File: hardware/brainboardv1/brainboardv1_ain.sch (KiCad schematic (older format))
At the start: 27 parts

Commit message: Nearly finished v1 sch & brd, await final check
Fixed errors from Rev 0, added MPU-6050 accelerometer/gyro for head
motion tracking, switched to +/-2.5V analog supply, added 2 bipolar
analog inputs for EOG tracking, added daisy-chain capability
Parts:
- removed P?: CONN_12, ~, symbol CONN_12
- added C55, C56: 4.7nF, ~, symbol C
- added P2: CONN_14, ~, symbol CONN_14
- added R21, R23: 4.99K, ~, symbol R
- gave numbers to parts that had none: 26
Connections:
- net labels added: +2.5V, -2.5V, CH1ELEC_N, CH2ELEC_N
- net labels removed: +5VA, AIN3N, AIN4N, AIN5N, AIN6N, AIN7N, AIN8N
- wire segments 67 -> 78
- no-connect marks 10 -> 1
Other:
- note added: "Channels 3-8 are single-ended only. Channels 1 and 2 can be configured as bipolar\nfor auxilliary signals like EOG, EMG, ECG, etc."
- note removed: "Rev. 0 is single-ended only. This saves board space\nand appears to be the dominant EEG BCI mode in any\ncase."
- moved on the sheet: C20, C21, C22, C23, C24, C25, C26, C27, C28, R11, R12, R13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

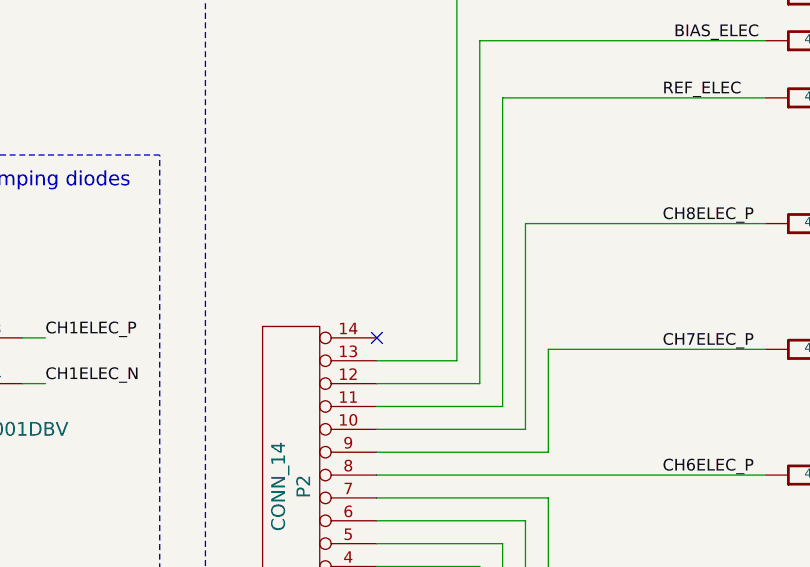
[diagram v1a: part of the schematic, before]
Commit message: Added thicker power traces and fixed silkscreen
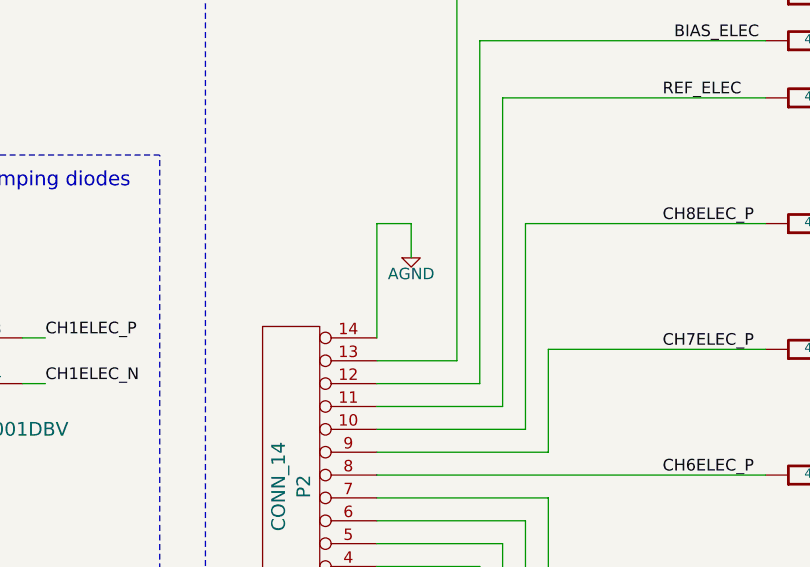
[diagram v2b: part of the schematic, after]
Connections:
- net AGND: now also P2.14 (P14)
- no-connect marks 1 -> 0
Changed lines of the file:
@@
 Sheet 2 7
 Title "BrainBoard: Open-Source Hardware for Wearable BCI"
-Date "27 dec 2013"
+Date "30 dec 2013"
 Rev "0"
 Comp "Virginia Commonwealth University"
@@
 Text Label 7800 6250 0    51   ~ 0
 CH1ELEC_N
-NoConn ~ 6550 2900
 Text Label 7800 5700 0    51   ~ 0
 CH2ELEC_N
@@
 	8800 6650 8800 6550
 Connection ~ 9200 6450
+Wire Wire Line
+	6550 2900 6550 2400
+Wire Wire Line
+	6550 2400 6700 2400
+Wire Wire Line
+	6700 2400 6700 2550
+$Comp
+L AGND #PWR029
+U 1 1 52C1B584
+P 6700 2550
+F 0 "#PWR029" H 6700 2550 40  0001 C CNN
+F 1 "AGND" H 6700 2480 50  0000 C CNN
+F 2 "" H 6700 2550 60  0000 C CNN
+F 3 "" H 6700 2550 60  0000 C CNN
+	1    6700 2550
+	1    0    0    -1
+$EndComp
 $EndSCHEMATC
